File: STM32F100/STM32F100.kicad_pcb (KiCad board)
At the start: 2 copper layers, 7.5 x 2 mm, 6 parts, among them J1 USB_OTG, J2 Screw_Terminal_01x02, U1 STM32F100C4Tx, Y1 8MHz

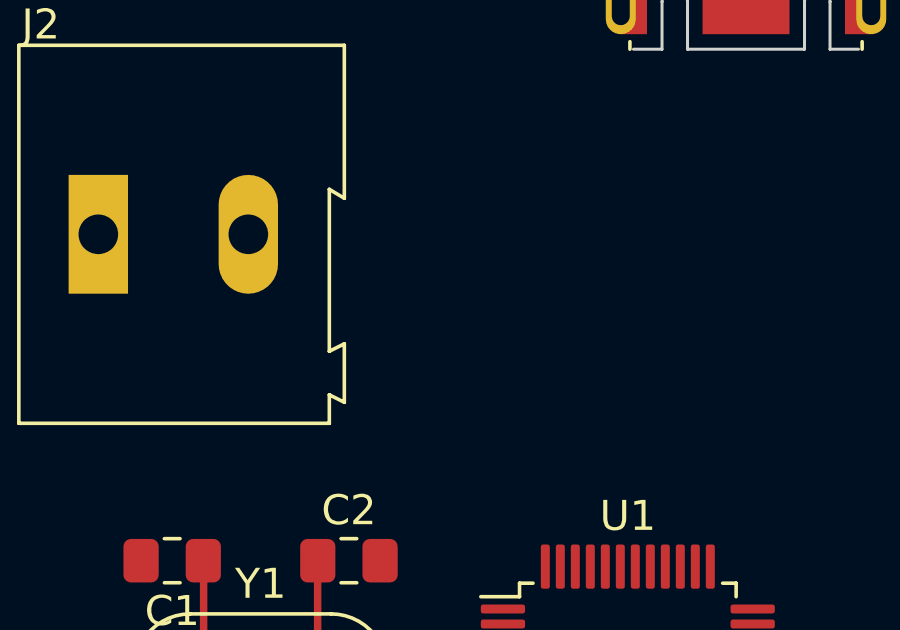
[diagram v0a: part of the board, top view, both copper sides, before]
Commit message: Add AMS1117 3.3V
add 3.3V voltage regulator
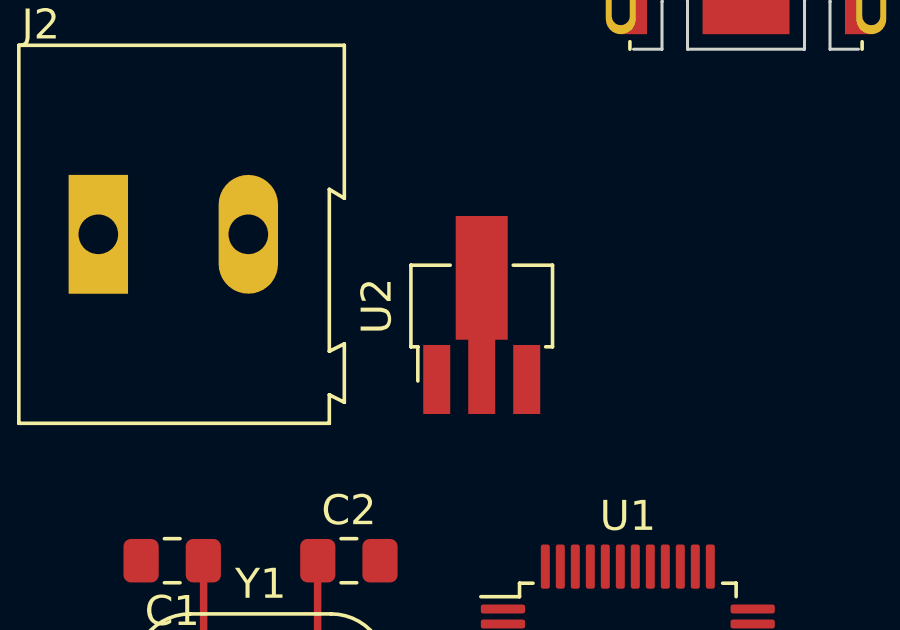
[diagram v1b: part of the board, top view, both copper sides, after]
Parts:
- added U2: AZ1117-3.3, Package_TO_SOT_SMD:SOT-89-3_Handsoldering, F.Cu at (139.8, 61.1)
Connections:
- U1 pad 23: unconnected-(U1-Pad23) -> GND
- U1 pad 35: unconnected-(U1-Pad35) -> GND
- U1 pad 47: unconnected-(U1-Pad47) -> GND
- U1 pad 8: unconnected-(U1-Pad8) -> GND
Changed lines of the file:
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@@
   (net 10 "unconnected-(U1-Pad4)")
   (net 11 "unconnected-(U1-Pad7)")
-  (net 12 "unconnected-(U1-Pad8)")
+  (net 12 "Net-(C2-Pad1)")
   (net 13 "unconnected-(U1-Pad9)")
   (net 14 "unconnected-(U1-Pad10)")
@@
   (net 25 "unconnected-(U1-Pad21)")
   (net 26 "unconnected-(U1-Pad22)")
-  (net 27 "unconnected-(U1-Pad23)")
+  (net 27 "unconnected-(U2-Pad1)")
   (net 28 "unconnected-(U1-Pad24)")
   (net 29 "unconnected-(U1-Pad25)")
@@
   (net 37 "unconnected-(U1-Pad33)")
   (net 38 "unconnected-(U1-Pad34)")
-  (net 39 "unconnected-(U1-Pad35)")
+  (net 39 "unconnected-(U2-Pad2)")
   (net 40 "unconnected-(U1-Pad36)")
   (net 41 "unconnected-(U1-Pad39)")
@@
   (net 47 "unconnected-(U1-Pad45)")
   (net 48 "unconnected-(U1-Pad46)")
-  (net 49 "unconnected-(U1-Pad47)")
+  (net 49 "unconnected-(U2-Pad3)")
   (net 50 "unconnected-(U1-Pad48)")
   (net 51 "Net-(C1-Pad1)")
-  (net 52 "Net-(Y1-Pad2)")
-  (net 53 "unconnected-(U1-Pad38)")
-  (net 54 "unconnected-(U1-Pad37)")
+  (net 52 "unconnected-(U1-Pad38)")
+  (net 53 "unconnected-(U1-Pad37)")
+  (footprint "Package_TO_SOT_SMD:SOT-89-3_Handsoldering" (layer "F.Cu")
+    (at 139.78 61.11 90)
+    (descr "SOT-89-3 Handsoldering")
+    (tags "SOT-89-3 Handsoldering")
+    (property "Sheetfile" "File: STM32F100.kicad_sch")
+    (property "Sheetname" "")
+    (attr smd)
+    (fp_text reference "U2" (at 0.3 -3.5 90) (layer "F.SilkS")
+      (effects (font (size 1 1) (thickness 0.15)))
+    )
+    (fp_text value "AZ1117-3.3" (at 0.3 3.5 90) (layer "F.Fab")
+      (effects (font (size 1 1) (thickness 0.15)))
+    )
+    (fp_text user "${REFERENCE}" (at 0.5 0) (layer "F.Fab")
+      (effects (font (size 1 1) (thickness 0.15)))
+    )
+    (fp_line (start -1.06 -2.36) (end -1.06 -2.13) (layer "F.SilkS") (width 0.12))
+    (fp_line (start -2.2 -2.13) (end -1.06 -2.13) (layer "F.SilkS") (width 0.12))
+    (fp_line (start 1.66 2.36) (end -1.06 2.36) (layer "F.SilkS") (width 0.12))
+    (fp_line (start 1.66 1.05) (end 1.66 2.36) (layer "F.SilkS") (width 0.12))
+    (fp_line (start 1.66 -2.36) (end 1.66 -1.05) (layer "F.SilkS") (width 0.12))
+    (fp_line (start -1.06 -2.36) (end 1.66 -2.36) (layer "F.SilkS") (width 0.12))
+    (fp_line (start -1.06 2.36) (end -1.06 2.13) (layer "F.SilkS") (width 0.12))
+    (fp_line (start -3.55 2.5) (end -3.55 -2.5) (layer "F.CrtYd") (width 0.05))
+    (fp_line (start -3.55 2.5) (end 3.55 2.5) (layer "F.CrtYd") (width 0.05))
+    (fp_line (start 3.55 -2.5) (end 3.55 2.5) (layer "F.CrtYd") (width 0.05))
+    (fp_line (start 3.55 -2.5) (end -3.55 -2.5) (layer "F.CrtYd") (width 0.05))
+    (fp_line (start 1.55 2.25) (end -0.95 2.25) (layer "F.Fab") (width 0.1))
+    (fp_line (start -0.95 -1.25) (end 0.05 -2.25) (layer "F.Fab") (width 0.1))
+    (fp_line (start -0.95 2.25) (end -0.95 -1.25) (layer "F.Fab") (width 0.1))
+    (fp_line (start 0.05 -2.25) (end 1.55 -2.25) (layer "F.Fab") (width 0.1))
+    (fp_line (start 1.55 -2.25) (end 1.55 2.25) (layer "F.Fab") (width 0.1))
+    (pad "1" smd rect (at -2.15 -1.5 90) (size 2.3 0.9) (layers "F.Cu" "F.Paste" "F.Mask")
+      (net 27 "unconnected-(U2-Pad1)") (pinfunction "GND") (pintype "power_in"))
+    (pad "2" smd custom (at -2.0625 0 90) (size 2.475 0.9) (layers "F.Cu" "F.Paste" "F.Mask")
+      (net 39 "unconnected-(U2-Pad2)") (pinfunction "VO") (pintype "power_out") (zone_connect 2)
+      (options (clearance outline) (anchor rect))
+      (primitives
+        (gr_poly (pts
+            (xy 5.3625 0.8665)
+            (xy 1.2375 0.8665)
+            (xy 1.2375 -0.8665)
+            (xy 5.3625 -0.8665)
+          ) (width 0) (fill yes))
+      ))
+    (pad "3" smd rect (at -2.15 1.5 90) (size 2.3 0.9) (layers "F.Cu" "F.Paste" "F.Mask")
+      (net 49 "unconnected-(U2-Pad3)") (pinfunction "VI") (pintype "power_in"))
+    (model "${KICAD6_3DMODEL_DIR}/Package_TO_SOT_SMD.3dshapes/SOT-89-3.wrl"
+      (offset (xyz 0 0 0))
+      (scale (xyz 1 1 1))
+      (rotate (xyz 0 0 0))
+    )
+  )
   (footprint "TerminalBlock:TerminalBlock_Altech_AK300-2_P5.00mm" (layer "F.Cu")
     (at 127 58.42)
@@
     (fp_line (start 1 0.625) (end -1 0.625) (layer "F.Fab") (width 0.1))
     (pad "1" smd roundrect (at -1.0375 0) (size 1.175 1.45) (layers "F.Cu" "F.Paste" "F.Mask") (roundrect_rratio 0.212766)
-      (net 52 "Net-(Y1-Pad2)") (pintype "passive"))
+      (net 12 "Net-(C2-Pad1)") (pintype "passive"))
     (pad "2" smd roundrect (at 1.0375 0) (size 1.175 1.45) (layers "F.Cu" "F.Paste" "F.Mask") (roundrect_rratio 0.212766)
       (net 5 "GND") (pintype "passive"))
@@
       (net 51 "Net-(C1-Pad1)") (pinfunction "1") (pintype "passive"))
     (pad "2" thru_hole circle (at 3.8 0) (size 1.5 1.5) (drill 0.8) (layers *.Cu *.Mask)
-      (net 52 "Net-(Y1-Pad2)") (pinfunction "2") (pintype "passive"))
+      (net 12 "Net-(C2-Pad1)") (pinfunction "2") (pintype "passive"))
     (model "${KICAD6_3DMODEL_DIR}/Crystal.3dshapes/Crystal_HC52-U_Vertical.wrl"
       (offset (xyz 0 0 0))
@@
       (net 10 "unconnected-(U1-Pad4)") (pinfunction "PC15") (pintype "bidirectional"))
     (pad "5" smd roundrect (at -4.1625 -0.75) (size 1.475 0.3) (layers "F.Cu" "F.Paste" "F.Mask") (roundrect_rratio 0.25)
-      (net 52 "Net-(Y1-Pad2)") (pinfunction "PD0") (pintype "input"))
+      (net 12 "Net-(C2-Pad1)") (pinfunction "PD0") (pintype "input"))
     (pad "6" smd roundrect (at -4.1625 -0.25) (size 1.475 0.3) (layers "F.Cu" "F.Paste" "F.Mask") (roundrect_rratio 0.25)
       (net 51 "Net-(C1-Pad1)") (pinfunction "PD1") (pintype "input"))
@@
       (net 11 "unconnected-(U1-Pad7)") (pinfunction "NRST") (pintype "input"))
     (pad "8" smd roundrect (at -4.1625 0.75) (size 1.475 0.3) (layers "F.Cu" "F.Paste" "F.Mask") (roundrect_rratio 0.25)
-      (net 12 "unconnected-(U1-Pad8)") (pinfunction "VSSA") (pintype "power_in"))
+      (net 5 "GND") (pinfunction "VSSA") (pintype "power_in"))
     (pad "9" smd roundrect (at -4.1625 1.25) (size 1.475 0.3) (layers "F.Cu" "F.Paste" "F.Mask") (roundrect_rratio 0.25)
       (net 13 "unconnected-(U1-Pad9)") (pinfunction "VDDA") (pintype "power_in"))
@@
       (net 26 "unconnected-(U1-Pad22)") (pinfunction "PB11") (pintype "bidirectional"))
     (pad "23" smd roundrect (at 2.25 4.1625) (size 0.3 1.475) (layers "F.Cu" "F.Paste" "F.Mask") (roundrect_rratio 0.25)
-      (net 27 "unconnected-(U1-Pad23)") (pinfunction "VSS") (pintype "power_in"))
+      (net 5 "GND") (pinfunction "VSS") (pintype "power_in"))
     (pad "24" smd roundrect (at 2.75 4.1625) (size 0.3 1.475) (layers "F.Cu" "F.Paste" "F.Mask") (roundrect_rratio 0.25)
       (net 28 "unconnected-(U1-Pad24)") (pinfunction "VDD") (pintype "power_in"))
@@
       (net 38 "unconnected-(U1-Pad34)") (pinfunction "PA13") (pintype "bidirectional"))
     (pad "35" smd roundrect (at 4.1625 -2.25) (size 1.475 0.3) (layers "F.Cu" "F.Paste" "F.Mask") (roundrect_rratio 0.25)
-      (net 39 "unconnected-(U1-Pad35)") (pinfunction "VSS") (pintype "power_in"))
+      (net 5 "GND") (pinfunction "VSS") (pintype "power_in"))
     (pad "36" smd roundrect (at 4.1625 -2.75) (size 1.475 0.3) (layers "F.Cu" "F.Paste" "F.Mask") (roundrect_rratio 0.25)
       (net 40 "unconnected-(U1-Pad36)") (pinfunction "VDD") (pintype "power_in"))
     (pad "37" smd roundrect (at 2.75 -4.1625) (size 0.3 1.475) (layers "F.Cu" "F.Paste" "F.Mask") (roundrect_rratio 0.25)
-      (net 54 "unconnected-(U1-Pad37)") (pinfunction "PA14") (pintype "bidirectional"))
+      (net 53 "unconnected-(U1-Pad37)") (pinfunction "PA14") (pintype "bidirectional"))
     (pad "38" smd roundrect (at 2.25 -4.1625) (size 0.3 1.475) (layers "F.Cu" "F.Paste" "F.Mask") (roundrect_rratio 0.25)
-      (net 53 "unconnected-(U1-Pad38)") (pinfunction "PA15") (pintype "bidirectional"))
+      (net 52 "unconnected-(U1-Pad38)") (pinfunction "PA15") (pintype "bidirectional"))
     (pad "39" smd roundrect (at 1.75 -4.1625) (size 0.3 1.475) (layers "F.Cu" "F.Paste" "F.Mask") (roundrect_rratio 0.25)
       (net 41 "unconnected-(U1-Pad39)") (pinfunction "PB3") (pintype "bidirectional"))
@@
       (net 48 "unconnected-(U1-Pad46)") (pinfunction "PB9") (pintype "bidirectional"))
     (pad "47" smd roundrect (at -2.25 -4.1625) (size 0.3 1.475) (layers "F.Cu" "F.Paste" "F.Mask") (roundrect_rratio 0.25)
-      (net 49 "unconnected-(U1-Pad47)") (pinfunction "VSS") (pintype "power_in"))
+      (net 5 "GND") (pinfunction "VSS") (pintype "power_in"))
     (pad "48" smd roundrect (at -2.75 -4.1625) (size 0.3 1.475) (layers "F.Cu" "F.Paste" "F.Mask") (roundrect_rratio 0.25)
       (net 50 "unconnected-(U1-Pad48)") (pinfunction "VDD") (pintype "power_in"))
@@
     )
   )
+  (segment (start 134.315 69.3) (end 134.3102 69.3048) (width 0.25) (layer "F.Cu") (net 12))
+  (segment (start 134.3102 69.3048) (end 134.3102 72.9234) (width 0.25) (layer "F.Cu") (net 12))
+  (segment (start 140.4741 72.9234) (end 134.3102 72.9234) (width 0.25) (layer "F.Cu") (net 12))
+  (segment (start 140.4875 72.91) (end 140.4741 72.9234) (width 0.25) (layer "F.Cu") (net 12))
   (segment (start 130.5 69.3) (end 130.5102 69.3102) (width 0.25) (layer "F.Cu") (net 51))
   (segment (start 132.4634 72.9234) (end 130.5102 72.9234) (width 0.25) (layer "F.Cu") (net 51))
@@
   (segment (start 130.5102 69.3102) (end 130.5102 72.9234) (width 0.25) (layer "F.Cu") (net 51))
   (segment (start 133.83 74.29) (end 132.4634 72.9234) (width 0.25) (layer "F.Cu") (net 51))
-  (segment (start 134.315 69.3) (end 134.3102 69.3048) (width 0.25) (layer "F.Cu") (net 52))
-  (segment (start 134.3102 69.3048) (end 134.3102 72.9234) (width 0.25) (layer "F.Cu") (net 52))
-  (segment (start 140.4741 72.9234) (end 134.3102 72.9234) (width 0.25) (layer "F.Cu") (net 52))
-  (segment (start 140.4875 72.91) (end 140.4741 72.9234) (width 0.25) (layer "F.Cu") (net 52))
 )

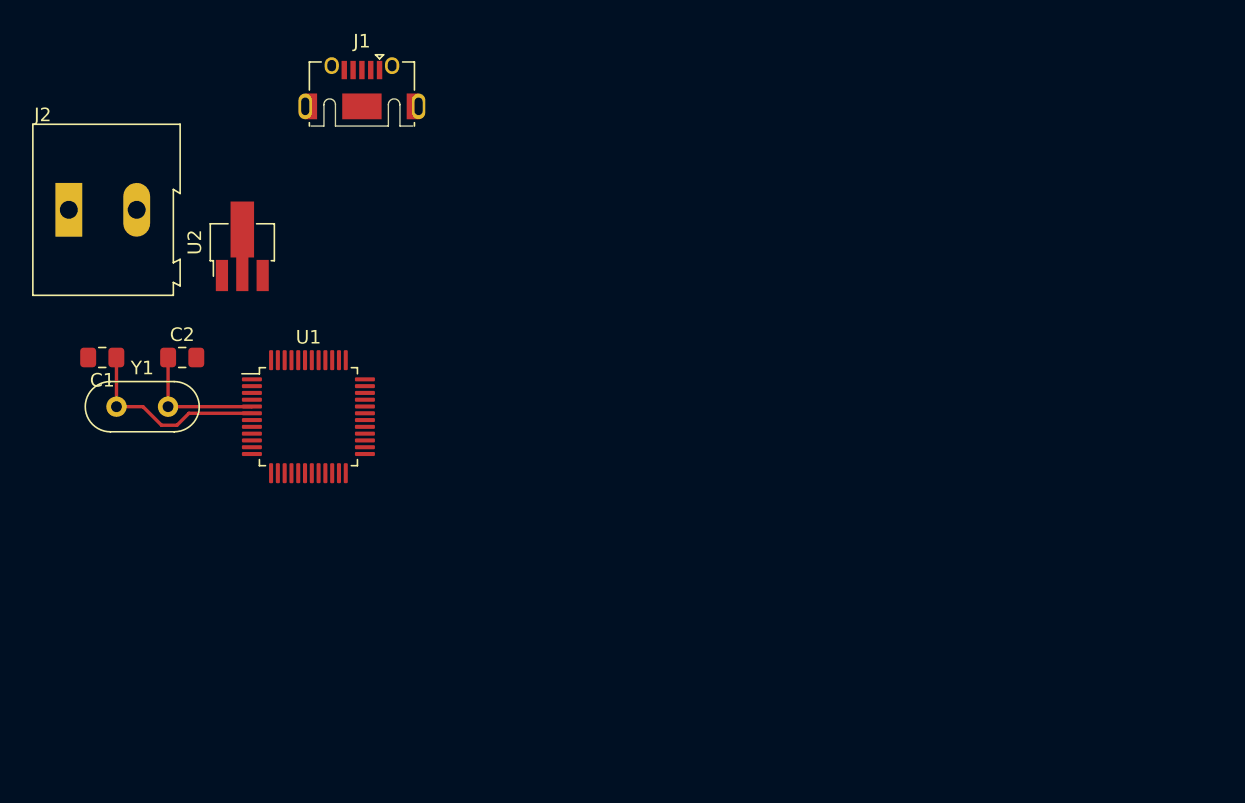
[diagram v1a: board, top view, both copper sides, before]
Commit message: Add IO pin header
Add IO Pinheader
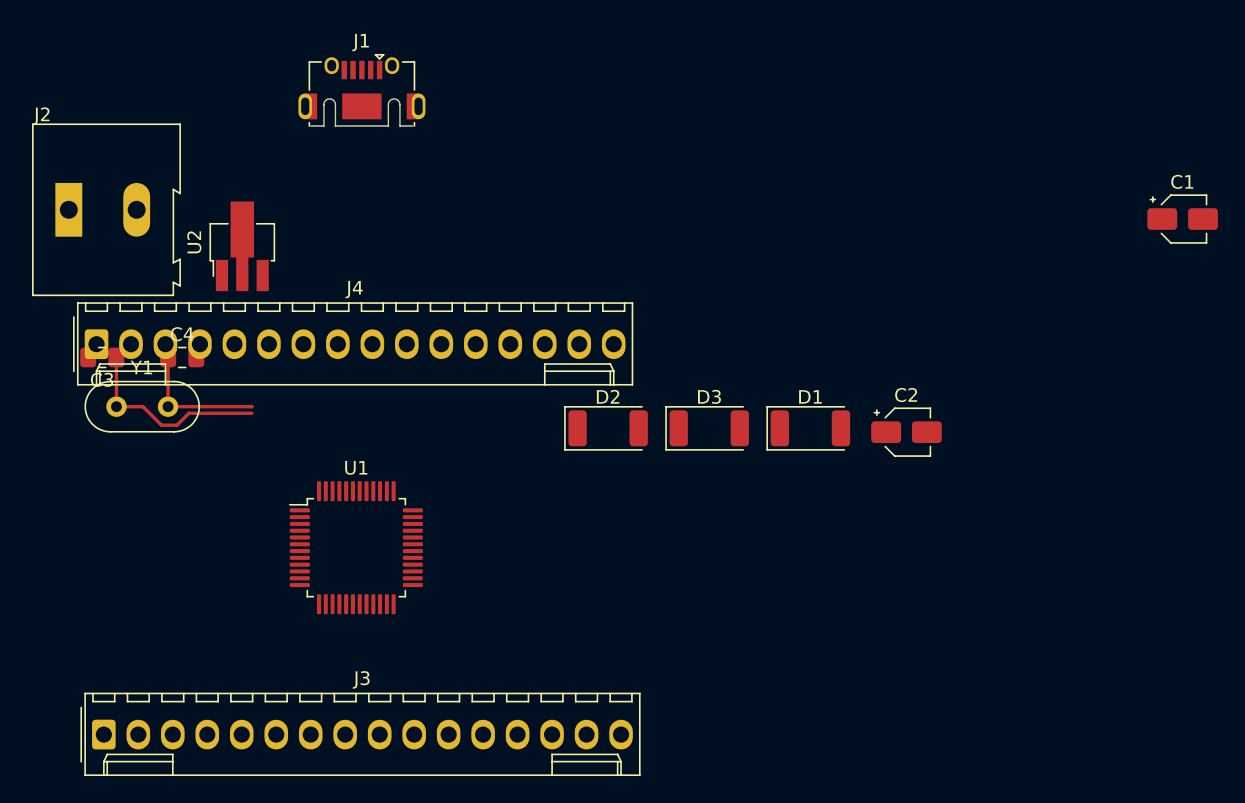
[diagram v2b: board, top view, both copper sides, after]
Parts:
- added C1: 10uF, Capacitor_SMD:CP_Elec_3x5.4, F.Cu at (209.1, 59.1)
- added C2: 10uF, Capacitor_SMD:CP_Elec_3x5.4, F.Cu at (188.7, 74.8)
- added D1: BAT60JFILM, Diode_SMD:D_2010_5025Metric, F.Cu at (181.6, 74.5)
- added D2: BAT60JFILM, Diode_SMD:D_2010_5025Metric, F.Cu at (166.7, 74.5)
- added D3: BAT60JFILM, Diode_SMD:D_2010_5025Metric, F.Cu at (174.2, 74.5)
- added J3: Conn_01x16, Connector_Molex:Molex_KK-254_AE-6410-16A_1x16_P2.54mm_Vertical, F.Cu at (129.6, 97.1)
- added J4: Conn_01x16, Connector_Molex:Molex_KK-254_AE-6410-16A_1x16_P2.54mm_Vertical, F.Cu at (129.0, 68.3)
- moved U1 10.3 mm to (148.2, 83.3)
- renumbered C1 to C3, C2 to C4
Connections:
- J2 pad 2: unconnected-(J2-Pad2) -> Net-(D1-Pad2)
- U1 pad 10: unconnected-(U1-Pad10) -> Net-(U1-Pad10)
- U1 pad 11: unconnected-(U1-Pad11) -> Net-(U1-Pad11)
- U1 pad 12: unconnected-(U1-Pad12) -> Net-(U1-Pad12)
- U1 pad 13: unconnected-(U1-Pad13) -> Net-(U1-Pad13)
- U1 pad 14: unconnected-(U1-Pad14) -> Net-(U1-Pad14)
- U1 pad 15: unconnected-(U1-Pad15) -> Net-(U1-Pad15)
- U1 pad 16: unconnected-(U1-Pad16) -> Net-(U1-Pad16)
- U1 pad 17: unconnected-(U1-Pad17) -> Net-(U1-Pad17)
- U1 pad 18: unconnected-(U1-Pad18) -> Net-(J4-Pad1)
- U1 pad 19: unconnected-(U1-Pad19) -> Net-(J4-Pad2)
- U1 pad 20: unconnected-(U1-Pad20) -> Net-(J4-Pad3)
- U1 pad 21: unconnected-(U1-Pad21) -> Net-(U1-Pad21)
- U1 pad 22: unconnected-(U1-Pad22) -> Net-(U1-Pad22)
- U1 pad 24: unconnected-(U1-Pad24) -> VDD
- U1 pad 25: unconnected-(U1-Pad25) -> Net-(U1-Pad25)
- U1 pad 26: unconnected-(U1-Pad26) -> Net-(U1-Pad26)
- U1 pad 27: unconnected-(U1-Pad27) -> Net-(U1-Pad27)
- U1 pad 28: unconnected-(U1-Pad28) -> Net-(U1-Pad28)
- U1 pad 29: unconnected-(U1-Pad29) -> Net-(U1-Pad29)
- U1 pad 30: unconnected-(U1-Pad30) -> Net-(U1-Pad30)
- U1 pad 31: unconnected-(U1-Pad31) -> Net-(J3-Pad11)
- U1 pad 32: unconnected-(U1-Pad32) -> Net-(J3-Pad12)
- U1 pad 33: unconnected-(U1-Pad33) -> Net-(J3-Pad13)
- U1 pad 34: unconnected-(U1-Pad34) -> Net-(U1-Pad34)
- U1 pad 36: unconnected-(U1-Pad36) -> VDD
- U1 pad 37: unconnected-(U1-Pad37) -> Net-(U1-Pad37)
- U1 pad 38: unconnected-(U1-Pad38) -> Net-(J3-Pad16)
- U1 pad 39: unconnected-(U1-Pad39) -> Net-(J4-Pad4)
- U1 pad 40: unconnected-(U1-Pad40) -> Net-(J4-Pad5)
- U1 pad 41: unconnected-(U1-Pad41) -> Net-(U1-Pad41)
- U1 pad 42: unconnected-(U1-Pad42) -> Net-(U1-Pad42)
- U1 pad 43: unconnected-(U1-Pad43) -> Net-(U1-Pad43)
- U1 pad 45: unconnected-(U1-Pad45) -> Net-(U1-Pad45)
- U1 pad 46: unconnected-(U1-Pad46) -> Net-(U1-Pad46)
- U1 pad 48: unconnected-(U1-Pad48) -> VDD
- U2 pad 1: unconnected-(U2-Pad1) -> GND
- U2 pad 2: unconnected-(U2-Pad2) -> +3.3V
- U2 pad 3: unconnected-(U2-Pad3) -> Net-(U2-Pad3)
